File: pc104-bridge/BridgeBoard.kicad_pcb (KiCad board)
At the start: 2 copper layers, 73.7 x 34.3 mm, 2 parts

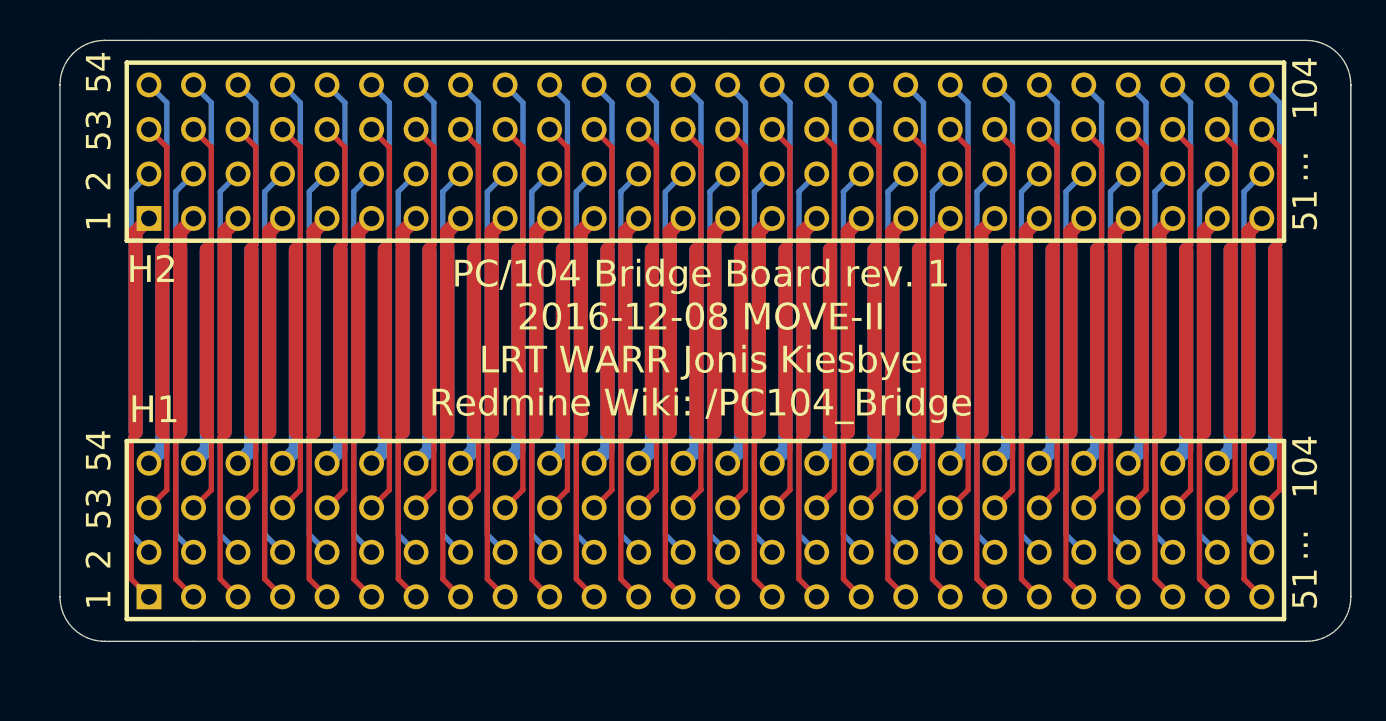
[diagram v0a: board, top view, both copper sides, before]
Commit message: adapt bridge and breakout to jlcpcb tolerance, add pin numbers to mainboard
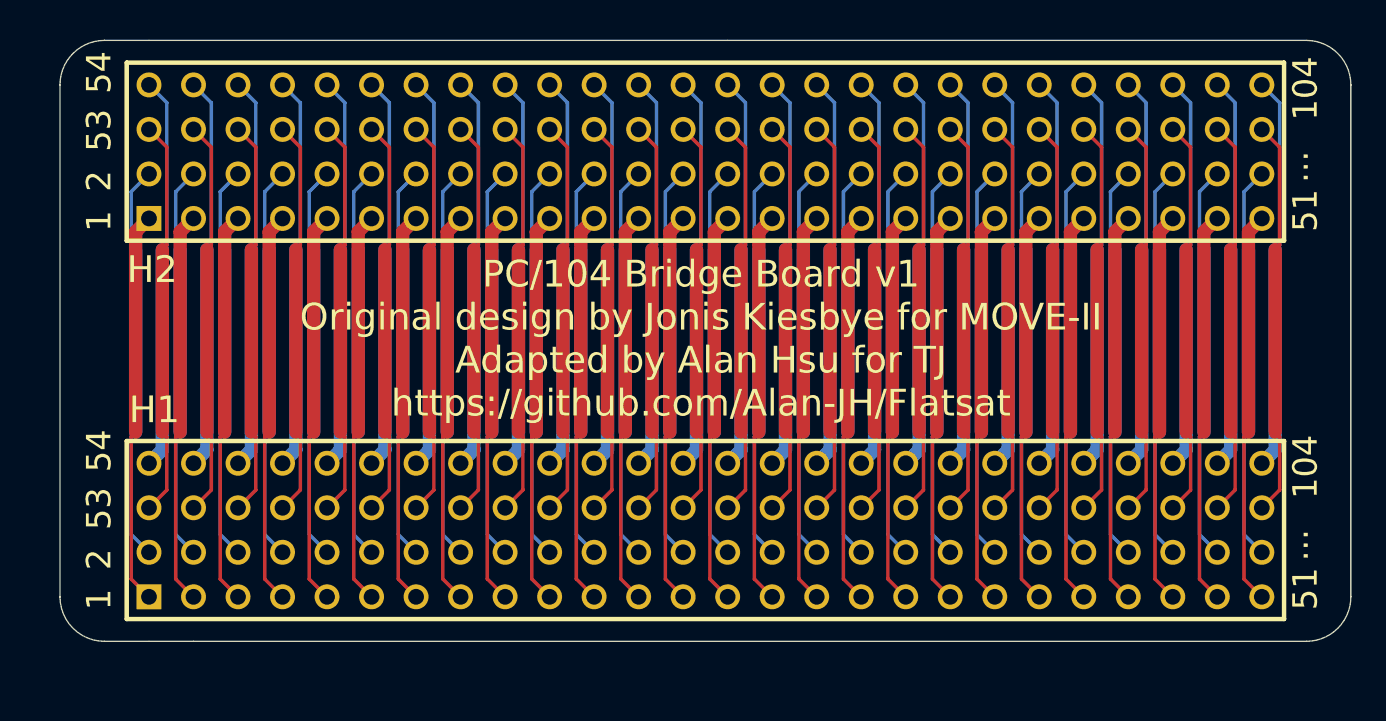
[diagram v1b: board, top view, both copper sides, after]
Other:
- board text added: "PC/104 Bridge Board v1 Original design by Jonis Kiesbye for MOVE-II Adapted by Alan Hsu for TJ https://github.com/Alan-JH/Flatsat"
- board text removed: "PC/104 Bridge Board rev. 1 2016-12-08 MOVE-II LRT WARR Jonis Kiesbye Redmine Wiki: /PC104_Bridge"

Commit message: fix board edge
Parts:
- moved H1 2.90 mm to (115.4, 122.1)
- moved H2 2.90 mm to (115.4, 100.6)
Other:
- board size 73.7 x 34.3 mm -> 73.5 x 34.3 mm
